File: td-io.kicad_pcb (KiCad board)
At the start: 2 copper layers, 189 x 93 mm, 70 parts, among them J1 USB_A, J2 USB_B, J3 JAMMA_Edge, J4 AudioJack3, J5 DB15_Male_HighDensity, J6 Conn_02x04_Top_Bottom, J7 Conn_02x17_Odd_Even, Q1 Si7141DP, Q2 FDS6930A, Q3 FDS6930A, SW1 SW_DIP_x02, U1 LM4950TS, U10 Pico, U2 ST485EB, U3 AD813, U4 74LS86, U5 AD813, U6 74LV166, U7 LM25085MM, U8 74LV166, U9 74LV166

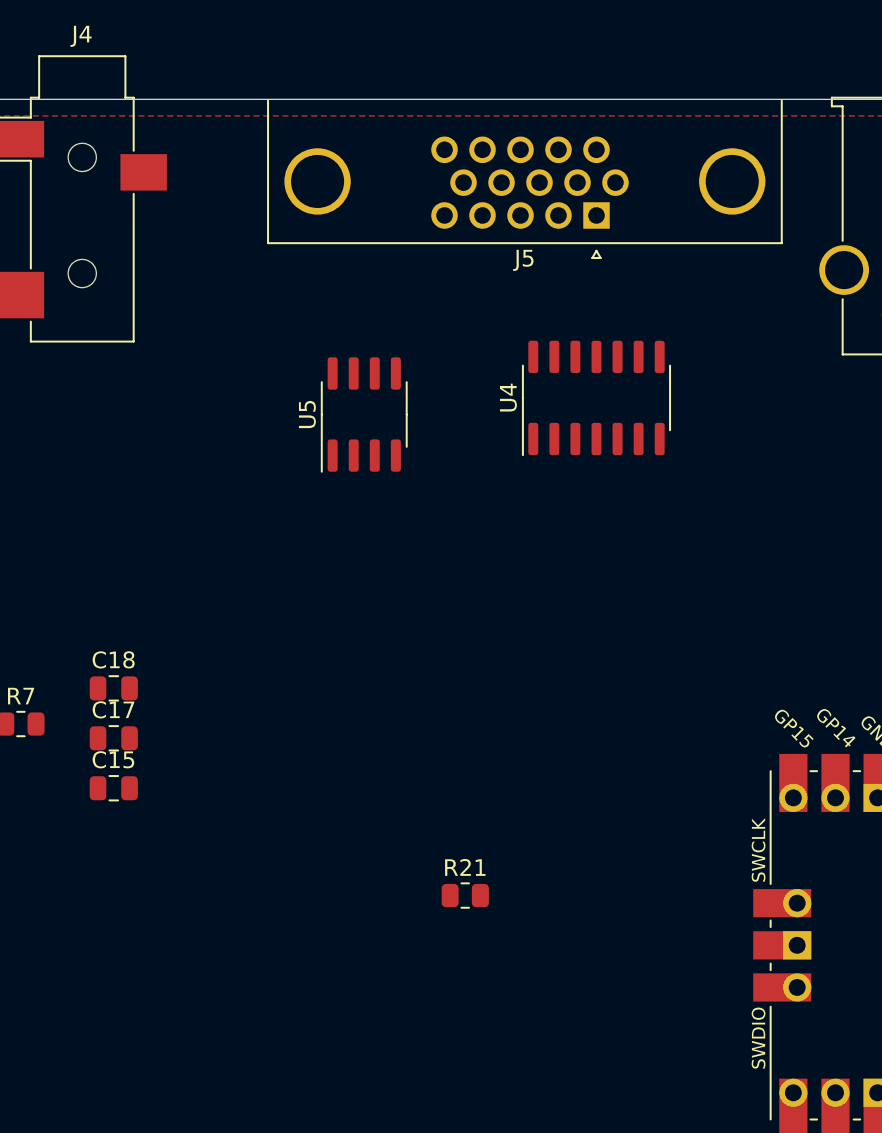
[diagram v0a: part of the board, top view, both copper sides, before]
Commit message: Swap male to female VGA connector
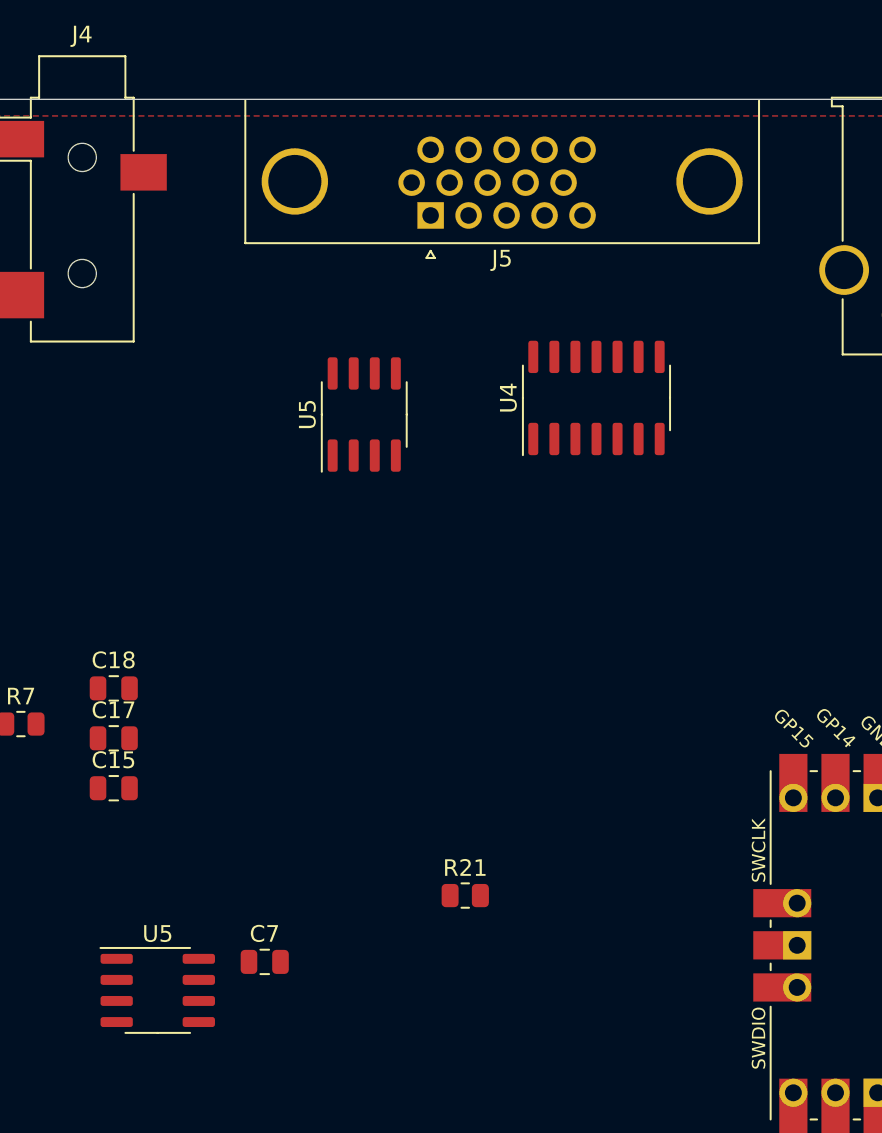
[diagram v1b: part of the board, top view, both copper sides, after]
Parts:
- added C7: 0.1uF, Capacitor_SMD:C_0805_2012Metric, F.Cu at (179.0, 117.0)
- added U5: AD813, Package_SO:SOIC-8_3.9x4.9mm_P1.27mm, F.Cu at (172.6, 118.7)
- J5: value DB15_Male_HighDensity -> DB15_Female_HighDensity; footprint Connector_Dsub:DSUB-15-HD_Male_Horizontal_P2.29x1.98mm_EdgePinOffset3.03mm_Housed_MountingHolesOffset4.94mm -> Connector_Dsub:DSUB-15-HD_Female_Horizontal_P2.29x1.98mm_EdgePinOffset3.03mm_Housed_MountingHolesOffset4.94mm
- moved J5 10.0 mm to (189.0, 72.0)

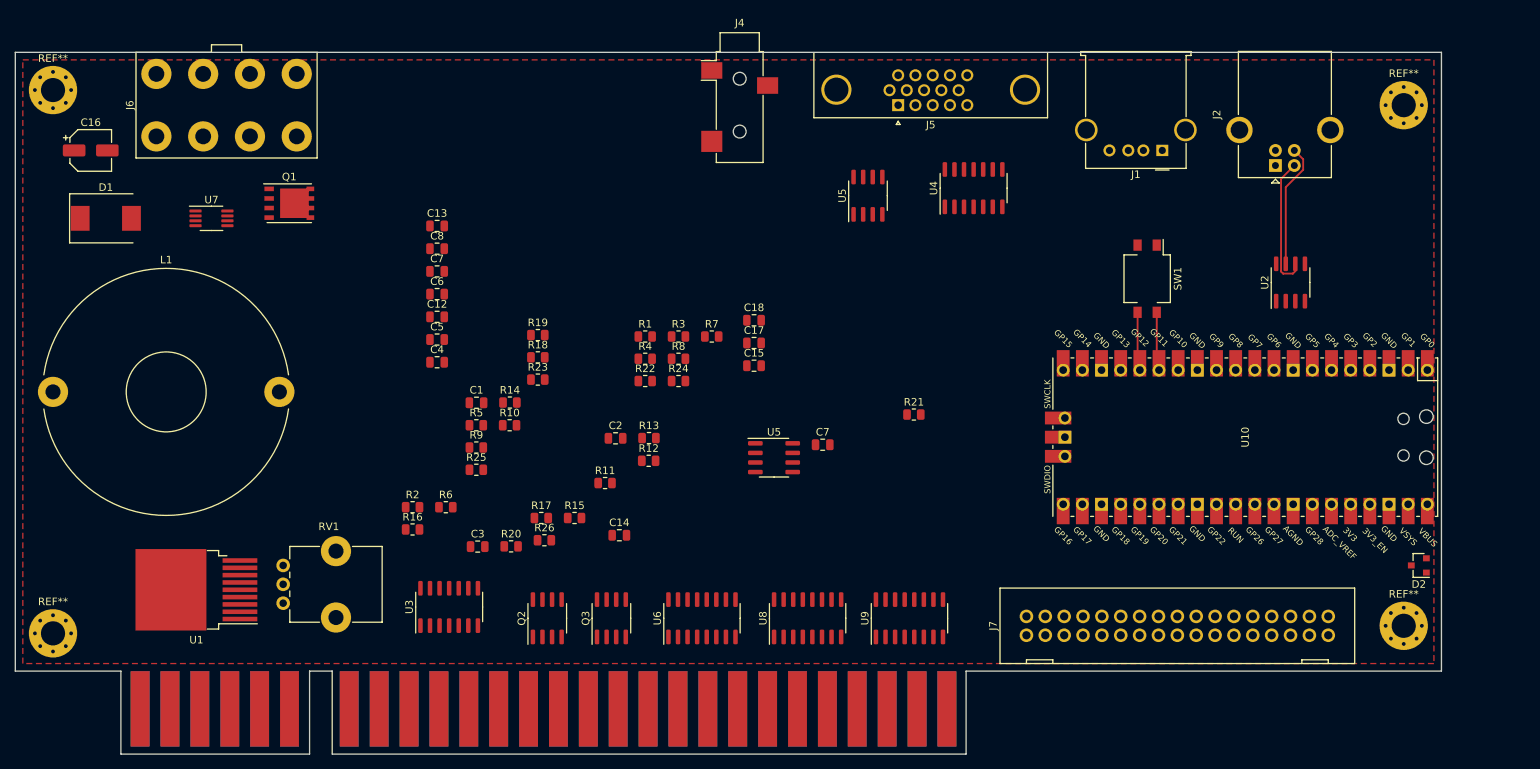
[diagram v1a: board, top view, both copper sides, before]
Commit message: Swap audio jacks out
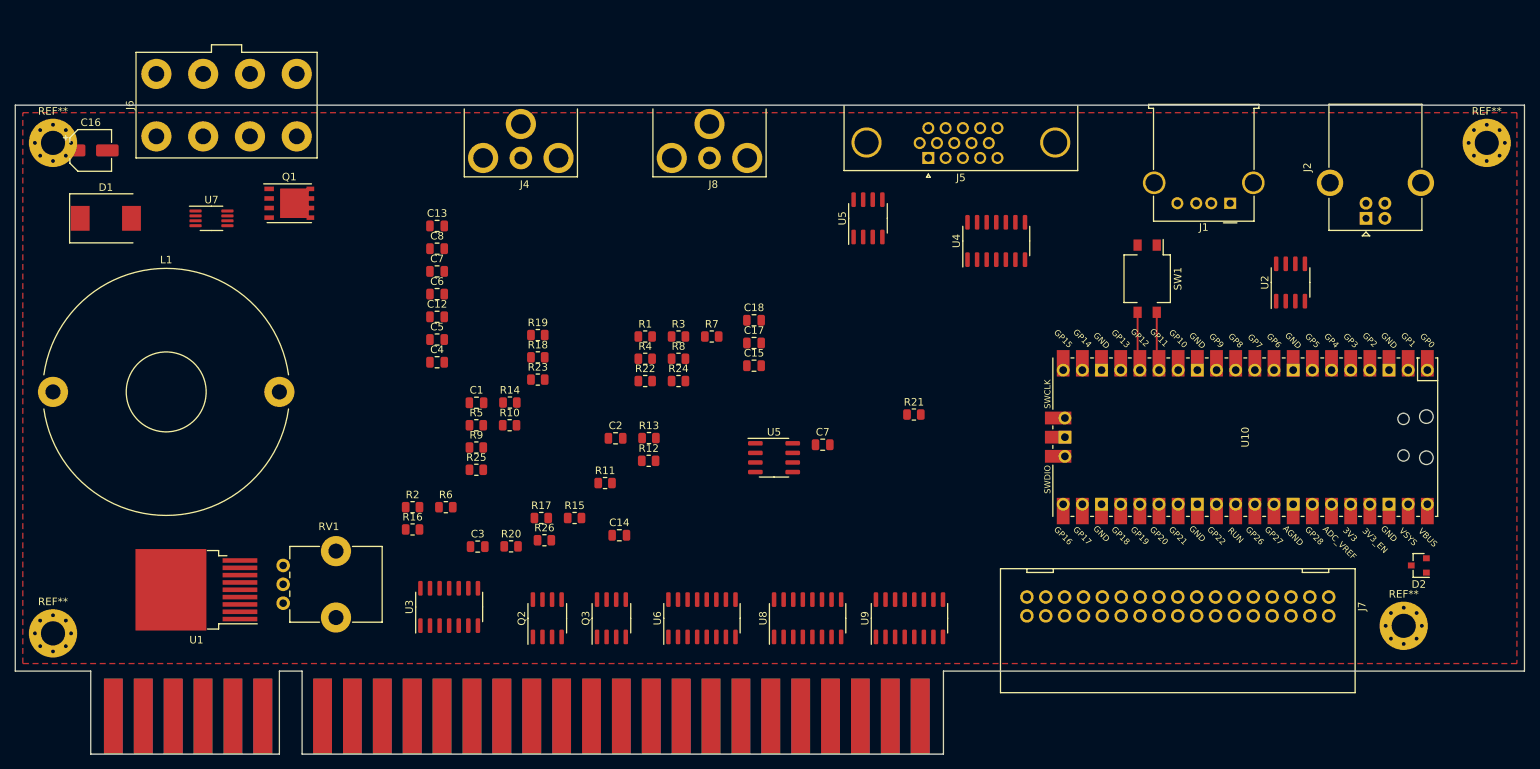
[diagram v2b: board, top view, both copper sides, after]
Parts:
- removed the REF** at (77.0, 70.0)
- removed the REF** at (256.0, 72.0)
- added J8: Conn_Coaxial, td-io:CUI_RCJ-01X, F.Cu at (164.0, 79.0)
- added REF**: MountingHole_3.2mm_M3_Pad_Via, MountingHole:MountingHole_3.2mm_M3_Pad_Via, F.Cu at (77.0, 77.0)
- added REF**: MountingHole_3.2mm_M3_Pad_Via, MountingHole:MountingHole_3.2mm_M3_Pad_Via, F.Cu at (267.0, 77.0)
- J4: value AudioJack3 -> Conn_Coaxial; footprint Connector_Audio:Jack_3.5mm_CUI_SJ-3523-SMT_Horizontal -> td-io:CUI_RCJ-01X
- J7: footprint td-io:DF1BZ-34DP-2.5DSA -> td-io:DF1BZ-34DP-2.5DS
- moved J4 30.1 mm to (139.0, 79.0)
- moved J2 13.9 mm to (251.0, 87.0)
- moved J1 11.4 mm to (233.0, 85.0)
- moved J5 8.06 mm to (193.0, 79.0)
- moved U4 7.62 mm to (202.0, 90.0)
- moved J3 3.68 mm to (138.5, 153.0)
- moved U5 3.00 mm to (185.0, 87.0)
- moved J7 2.57 mm to (226.1, 138.4), turned to 180 degrees
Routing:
- net Net-(J1-Pad2): track 17.9 -> 0.00 mm
- net Net-(J1-Pad3): track 16.5 -> 0.00 mm
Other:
- board size 189 x 93 mm -> 200 x 86 mm

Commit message: Add alternative power supply
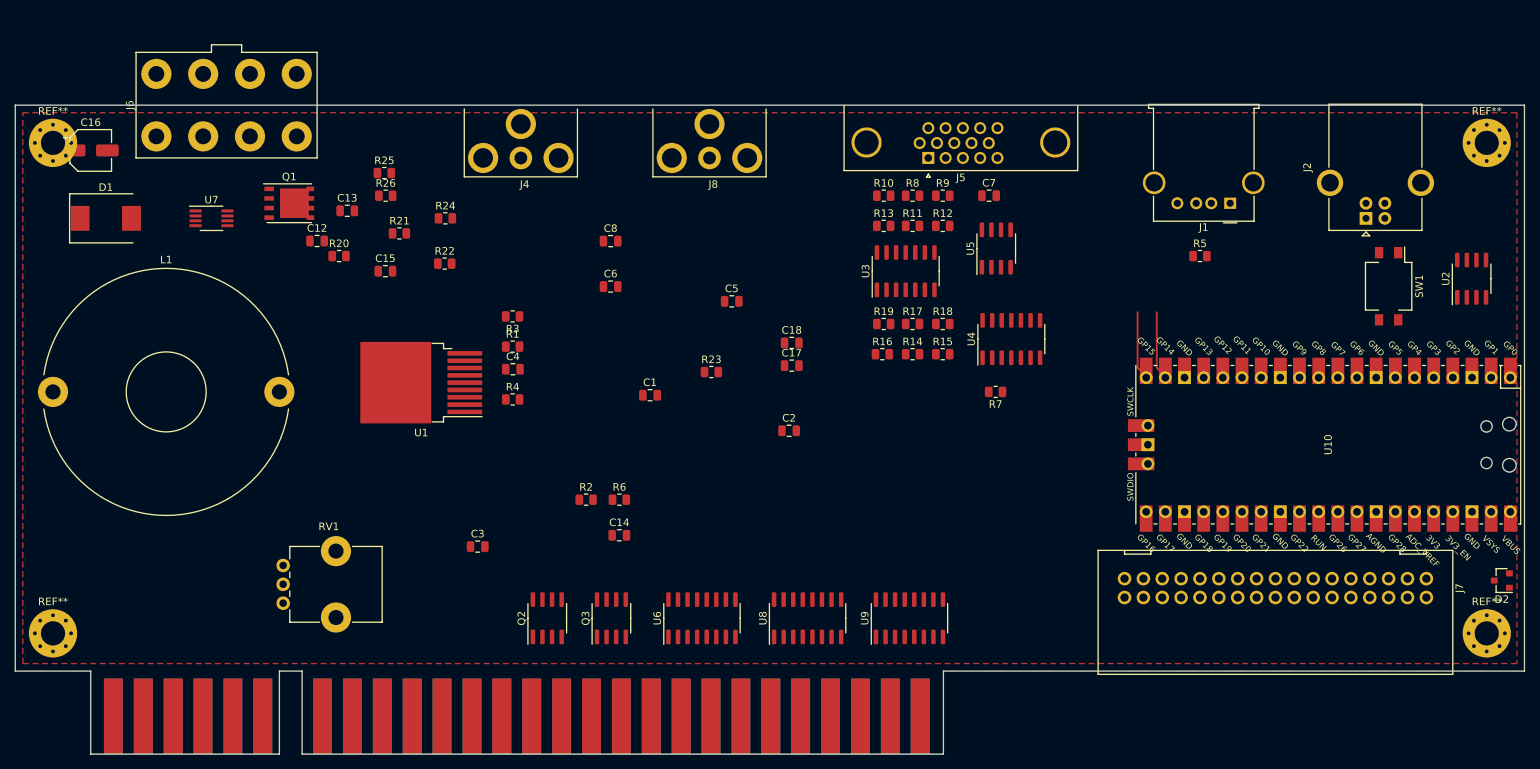
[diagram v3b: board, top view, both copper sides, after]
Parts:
- removed the C7 at (179.0, 117.0)
- removed the C7 at (127.9, 94.0)
- removed the U5 at (185.0, 87.0)
- added C7: 0.1uF, Capacitor_SMD:C_0805_2012Metric, F.Cu at (201.1, 84.0)
- U5: value AD813 -> AT24CS01-SSHM
- moved R5 98.5 mm to (229.0, 92.0)
- moved U3 75.1 mm to (190.0, 94.0)
- moved R21 72.3 mm to (122.9, 89.0)
- moved R9 70.2 mm to (194.9, 84.0)
- moved R16 66.5 mm to (186.9, 105.0)
- moved R10 58.2 mm to (187.1, 84.0)
- moved R17 55.5 mm to (190.9, 101.0)
- moved R18 53.8 mm to (194.9, 101.0)
- moved R14 53.7 mm to (190.9, 105.0)
- moved R15 53.4 mm to (194.9, 105.0)
- moved R11 53.1 mm to (190.9, 88.0)
- moved C15 50.4 mm to (121.0, 94.0)
- moved R26 50.3 mm to (121.1, 84.0)
- moved R12 49.9 mm to (194.9, 88.0)
- moved R19 45.9 mm to (187.1, 101.0)
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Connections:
- L1 pad 1: Net-(L1-Pad1) -> Net-(D1-Pad1)
- Q1 pad 5: Net-(L1-Pad1) -> Net-(Q1-Pad5)
- R22 pad 2: Net-(L1-Pad1) -> Net-(Q1-Pad5)
- U7 pad 5: Net-(L1-Pad1) -> Net-(Q1-Pad5)
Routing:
- net Net-(U10-Pad20): track 0.00 -> 7.78 mm
- net Net-(SW1-Pad3): track 7.78 -> 0.00 mm
- net Net-(U10-Pad19): track 0.00 -> 7.78 mm
- net Net-(SW1-Pad4): track 7.78 -> 0.00 mm

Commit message: Add JVS chaining support
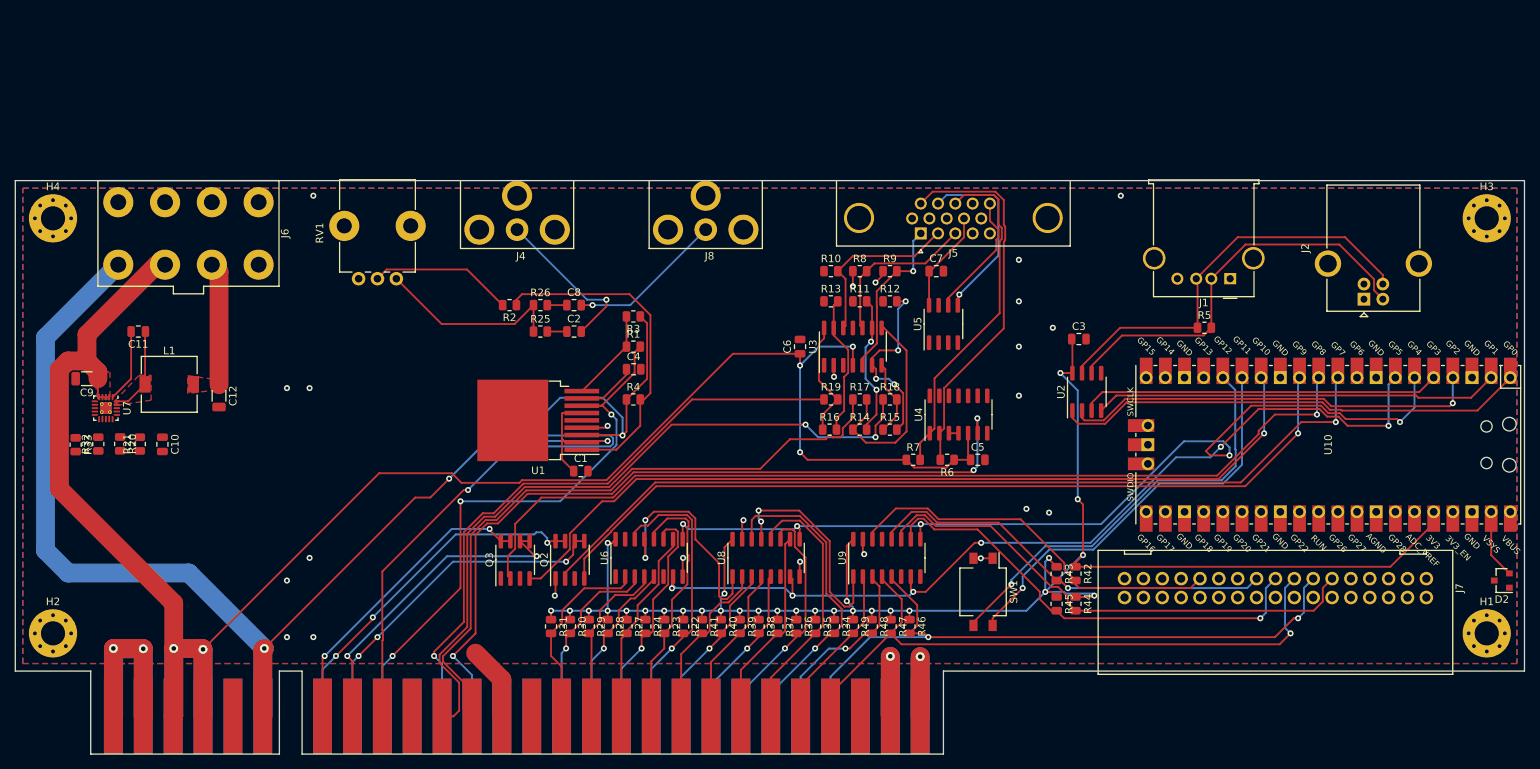
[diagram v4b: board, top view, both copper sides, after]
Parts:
- removed C13, C14: 10uF, Capacitor_SMD:C_0805_2012Metric
- removed C15: 750pF, Capacitor_SMD:C_0805_2012Metric
- removed C16: 100uF, Capacitor_SMD:CP_Elec_5x5.3
- removed C17: 1uF, Capacitor_SMD:C_0805_2012Metric
- removed C18: 1000pF, Capacitor_SMD:C_0805_2012Metric
- removed D1: SL44-E3/57T, Diode_SMD:D_SMC
- removed Q1: Si7141DP, Package_SO:PowerPAK_SO-8_Single
- removed REF** (x4): MountingHole_3.2mm_M3_Pad_Via, MountingHole:MountingHole_3.2mm_M3_Pad_Via
- added C10: 1uF, Capacitor_SMD:C_0805_2012Metric, F.Cu at (91.5, 117.0)
- added C11: 0.1uF, Capacitor_SMD:C_0805_2012Metric, F.Cu at (88.3, 102.0)
- added C9: 100uF, Capacitor_SMD:C_1206_3216Metric, F.Cu at (81.5, 108.2)
- added H1: MountingHole_Pad, MountingHole:MountingHole_3.2mm_M3_Pad_Via, F.Cu at (267.0, 142.0)
- added H2: MountingHole_Pad, MountingHole:MountingHole_3.2mm_M3_Pad_Via, F.Cu at (77.0, 142.0)
- added H3: MountingHole_Pad, MountingHole:MountingHole_3.2mm_M3_Pad_Via, F.Cu at (267.0, 87.0)
- added H4: MountingHole_Pad, MountingHole:MountingHole_3.2mm_M3_Pad_Via, F.Cu at (77.0, 87.0)
- added R27: 10k, Resistor_SMD:R_0805_2012Metric, F.Cu at (153.0, 141.1)
- added R28: 10k, Resistor_SMD:R_0805_2012Metric, F.Cu at (150.5, 141.1)
- added R29: 10k, Resistor_SMD:R_0805_2012Metric, F.Cu at (148.0, 141.1)
- added R30: 10k, Resistor_SMD:R_0805_2012Metric, F.Cu at (145.5, 141.1)
- added R31: 10k, Resistor_SMD:R_0805_2012Metric, F.Cu at (143.0, 141.1)
- added R32: 90k, Resistor_SMD:R_0805_2012Metric, F.Cu at (83.0, 116.9)
- added R33: 20k, Resistor_SMD:R_0805_2012Metric, F.Cu at (80.0, 117.0)
- added R34: 10k, Resistor_SMD:R_0805_2012Metric, F.Cu at (180.5, 141.1)
- added R35: 10k, Resistor_SMD:R_0805_2012Metric, F.Cu at (178.0, 141.1)
- added R36: 10k, Resistor_SMD:R_0805_2012Metric, F.Cu at (175.5, 141.1)
- added R37: 10k, Resistor_SMD:R_0805_2012Metric, F.Cu at (173.0, 141.1)
- added R38: 10k, Resistor_SMD:R_0805_2012Metric, F.Cu at (170.5, 141.1)
- added R39: 10k, Resistor_SMD:R_0805_2012Metric, F.Cu at (168.0, 141.1)
- added R40: 10k, Resistor_SMD:R_0805_2012Metric, F.Cu at (165.5, 141.1)
- added R41: 10k, Resistor_SMD:R_0805_2012Metric, F.Cu at (163.0, 141.1)
- added R42: 10k, Resistor_SMD:R_0805_2012Metric, F.Cu at (212.5, 134.1)
- added R43: 10k, Resistor_SMD:R_0805_2012Metric, F.Cu at (210.0, 134.1)
- added R44: 10k, Resistor_SMD:R_0805_2012Metric, F.Cu at (212.5, 138.1)
- added R45: 10k, Resistor_SMD:R_0805_2012Metric, F.Cu at (210.0, 138.1)
- added R46: 10k, Resistor_SMD:R_0805_2012Metric, F.Cu at (190.5, 141.1)
- added R47: 10k, Resistor_SMD:R_0805_2012Metric, F.Cu at (188.0, 141.1)
- added R48: 10k, Resistor_SMD:R_0805_2012Metric, F.Cu at (185.5, 141.1)
- added R49: 10k, Resistor_SMD:R_0805_2012Metric, F.Cu at (183.0, 141.1)
- C12: value 10uF -> 100uF; footprint Capacitor_SMD:C_0805_2012Metric -> Capacitor_SMD:C_1206_3216Metric
- L1: value 0.1mH -> 1uH; footprint Inductor_THT:L_Toroid_Horizontal_D32.5mm_P30.00mm_Bourns_2300 -> Inductor_SMD:L_7.3x7.3_H3.5
- R20: value 15.4k -> 160k
- R21: value 2.94k -> 51k
- R22: value 0.01 -> 10k
- R24: value 6.04k -> 10k
- U7: value LM25085MM -> TPS568230; footprint Package_SO:MSOP-8_3x3mm_P0.65mm -> Package_DFN_QFN:VQFN-20-1EP_3x3mm_P0.45mm_EP1.55x1.55mm_ThermalVias
- moved C3 84.3 mm to (212.9, 103.0)
- moved SW1 67.3 mm to (200.2, 136.5)
- moved R24 60.2 mm to (155.5, 141.1), turned to 270 degrees
- moved R22 57.5 mm to (160.5, 141.1), turned to 270 degrees
- moved U2 53.2 mm to (214.0, 110.0)
- moved RV1 45.5 mm to (122.5, 95.0), turned to 90 degrees
- moved R21 44.3 mm to (88.5, 116.9), turned to 90 degrees
- moved R6 43.8 mm to (195.5, 119.0), turned to 180 degrees
- moved C5 38.8 mm to (199.6, 119.0)
- moved R20 38.2 mm to (85.9, 116.9), turned to 270 degrees
- moved R23 34.3 mm to (158.0, 141.1), turned to 270 degrees
- moved C2 31.4 mm to (146.1, 102.0)
- moved R25 29.5 mm to (141.6, 102.0)
- moved U7 28.8 mm to (84.0, 112.2), turned to 270 degrees
- moved R2 27.7 mm to (137.5, 98.5), turned to 180 degrees
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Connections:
- C12 pad 1: +5V -> +3.3VP
- C12 pad 2: Net-(C12-Pad2) -> GND
- C3 pad 1: +5V -> +3V3
- J3 pad L: (no net) -> /speaker-
- J6 pad 2: +3V3 -> +3.3VP
- L1 pad 1: Net-(D1-Pad1) -> /SW
- L1 pad 2: +3V3 -> +3.3VP
- R20 pad 1: +5V -> Net-(C10-Pad1)
- R20 pad 2: Net-(C12-Pad2) -> Net-(R20-Pad2)
- R21 pad 1: Net-(C18-Pad1) -> Net-(R20-Pad2)
- R21 pad 2: +5V -> GND
- R22 pad 1: Net-(C18-Pad1) -> +3V3
- R22 pad 2: Net-(Q1-Pad5) -> /p2down
- R23 pad 2: Net-(C15-Pad2) -> /p1down
- R24 pad 1: Net-(C15-Pad2) -> +3V3
- R24 pad 2: GND -> /p2up
- U2 pad 8: +5V -> +3V3
- U6 pad 1: Net-(U6-Pad1) -> GND
- U6 pad 10: Net-(U6-Pad10) -> /p1up
- U6 pad 11: Net-(U6-Pad11) -> /p2up
- U6 pad 12: Net-(U6-Pad12) -> /p1down
- U6 pad 14: Net-(U6-Pad14) -> /p2down
- U6 pad 2: Net-(U6-Pad2) -> /c1
- U6 pad 3: Net-(U6-Pad3) -> /c2
- U6 pad 4: Net-(U6-Pad4) -> /p1start
- U6 pad 5: Net-(U6-Pad5) -> /p2start
- U7 pad 1: +5V -> Net-(C11-Pad2)
- U7 pad 2: Net-(C12-Pad2) -> +5V
- U7 pad 3: Net-(C15-Pad2) -> +5V
- U7 pad 4: GND -> +5V
- U7 pad 5: Net-(Q1-Pad5) -> +5V
- U7 pad 6: Net-(Q1-Pad4) -> /SW
- U7 pad 7: Net-(C17-Pad2) -> GND
- U7 pad 8: +5V -> GND
- U8 pad 10: Net-(U8-Pad10) -> /p1_1
- U8 pad 11: Net-(U8-Pad11) -> /p2_1
- U8 pad 12: Net-(U8-Pad12) -> /p1_2
- U8 pad 14: Net-(U8-Pad14) -> /p2_2
- U8 pad 2: Net-(U8-Pad2) -> /p1left
- U8 pad 3: Net-(U8-Pad3) -> /p2left
- U8 pad 4: Net-(U8-Pad4) -> /p1right
- U8 pad 5: Net-(U8-Pad5) -> /p2right
- U9 pad 10: Net-(U9-Pad10) -> /p1_5
- U9 pad 11: Net-(U9-Pad11) -> /p2_5
- U9 pad 12: Net-(U9-Pad12) -> /p1_6
- U9 pad 13: /sr_data -> Net-(U9-Pad13)
- U9 pad 14: Net-(U9-Pad14) -> /p2_6
- U9 pad 2: Net-(U9-Pad2) -> /p1_3
- U9 pad 3: Net-(U9-Pad3) -> /p2_3
- U9 pad 4: Net-(U9-Pad4) -> /p1_4
- U9 pad 5: Net-(U9-Pad5) -> /p2_4
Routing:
- net +5V: track 0.00 -> 263.0 mm, vias 0 -> 5
- net +3V3: track 0.00 -> 229.8 mm, vias 0 -> 29
- net +12V: track 0.00 -> 168.4 mm, vias 0 -> 4
- net /meter2_ctl: track 0.00 -> 125.3 mm, vias 0 -> 1
- net /sr_clr: track 0.00 -> 124.1 mm, vias 0 -> 5
- net /sr_clk: track 0.00 -> 121.5 mm, vias 0 -> 6
- net /meter1_ctl: track 0.00 -> 117.2 mm, vias 0 -> 1
- net /lockout2_ctl: track 0.00 -> 114.1 mm, vias 0 -> 1
- net /lockout1_ctl: track 0.00 -> 111.6 mm, vias 0 -> 1
- net /speaker+: track 0.00 -> 111.4 mm, vias 0 -> 2
- net GND: track 0.00 -> 108.5 mm, vias 0 -> 29
- net /jamma_sync: track 0.00 -> 105.0 mm, vias 0 -> 3
- net /jamma_red: track 0.00 -> 94.8 mm, vias 0 -> 2
- net /p2_4: track 0.00 -> 88.6 mm, vias 0 -> 2
- net /jamma_blue: track 0.00 -> 87.5 mm
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- added copper zone on F.Cu, net +3V3
- added copper zone on F.Cu, net +5V
- added copper zone on F.Cu, net /SW
- added copper zone on B.Cu, net GND
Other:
- board size 200 x 86 mm -> 200 x 76 mm
